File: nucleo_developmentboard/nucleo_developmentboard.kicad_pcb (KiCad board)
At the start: 2 copper layers, 91.4 x 69.8 mm, 30 parts, among them J1 Conn_01x03_Socket, J2 Conn_01x03_Socket, J3 Conn_01x02_Socket, J4 MOTOR2 OUT, J5 Conn_PinHeader_1x05_P2.54mm_V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, J6 MOTOR2 OUT, J7 Conn_01x01_Socket, J8 Conn_01x01_Socket, U1 NUCLEO-L432KC, U2 L293D, U3 LM7805_TO220, U4 HM-11_Module

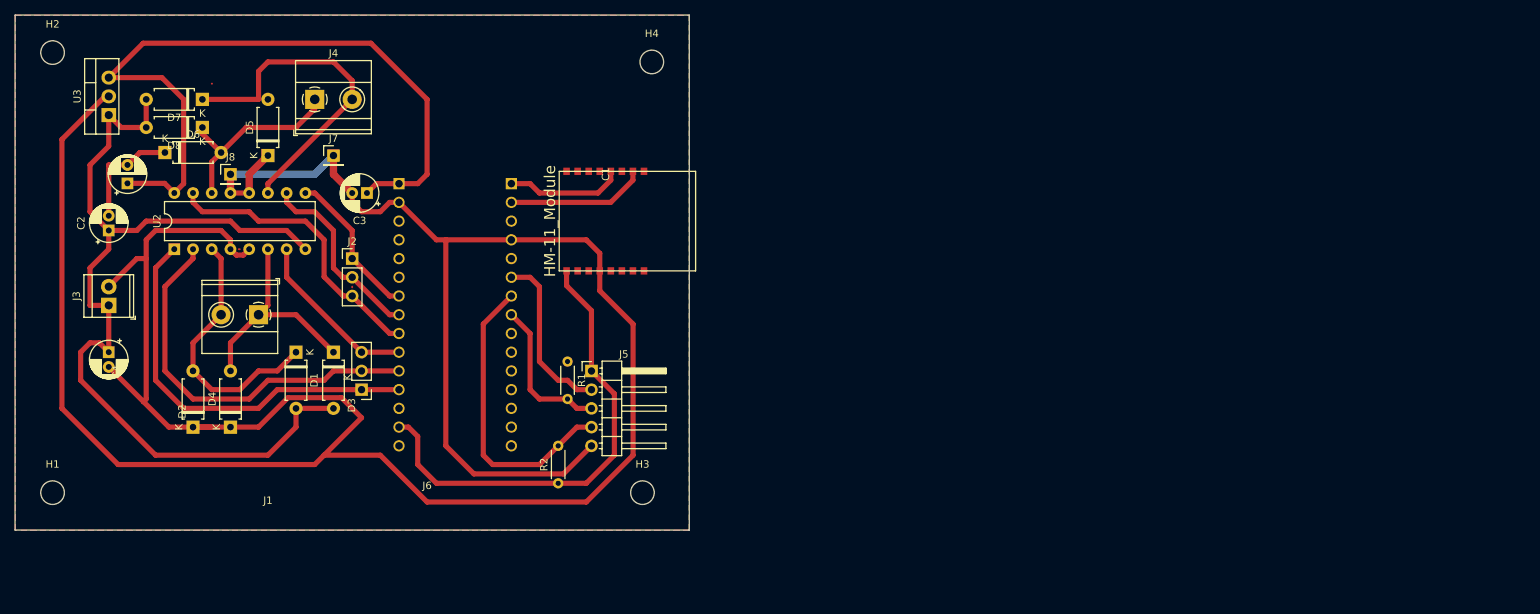
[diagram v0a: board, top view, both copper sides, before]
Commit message: updated Nucleo connections and switched to HM11 smd
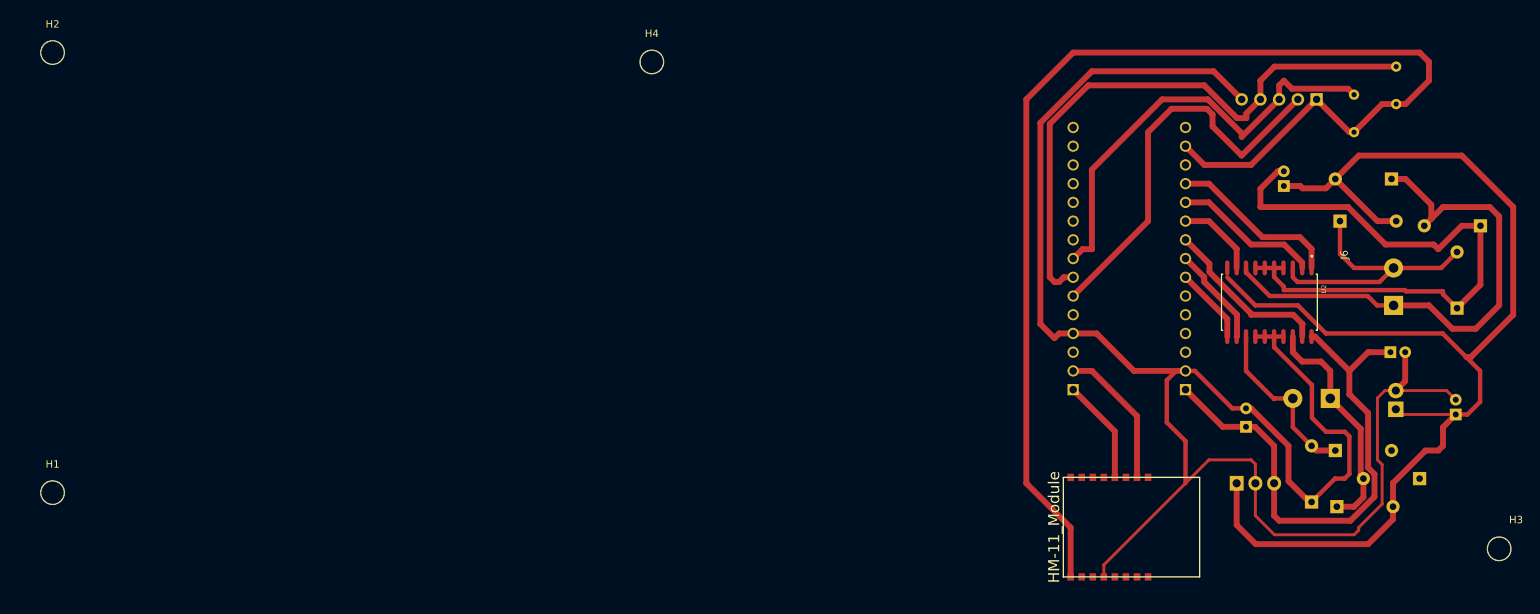
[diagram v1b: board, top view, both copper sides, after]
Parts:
- removed J1, J2: Conn_01x03_Socket, Connector_PinHeader_2.54mm:PinHeader_1x03_P2.54mm_Vertical
- removed J7, J8: Conn_01x01_Socket, Connector_PinHeader_2.54mm:PinHeader_1x01_P2.54mm_Vertical
- C1, C2, C3, C4, D1, D2, D3, D4, D5, D6, D7, D8, J3, J4, J5, J6, R1, R2, U3: moved to B.Cu
- U2: footprint Package_DIP:DIP-16_W7.62mm -> L293dd:SOIC127P1032X265-20N
- moved C2 184.4 mm to (250.0, 97.3)
- moved D6 175.8 mm to (245.1, 106.0), turned to 180 degrees
- moved J3 175.1 mm to (241.9, 96.6)
- moved D2 172.2 mm to (250.2, 82.9)
- moved D4 171.7 mm to (253.4, 71.8), turned to 180 degrees
- moved D8 162.2 mm to (233.9, 109.9), turned to 0 degrees
- moved C4 161.0 mm to (226.7, 66.4), turned to 90 degrees
- moved U3 160.9 mm to (220.3, 106.7), turned to 0 degrees
- moved D7 160.9 mm to (233.7, 102.2), turned to 0 degrees
- moved C1 155.3 mm to (221.6, 99.0)
- moved J6 154.0 mm to (241.6, 82.6), turned to 90 degrees
- moved D5 149.2 mm to (230.5, 109.2)
- moved U2 148.7 mm to (224.7, 82.1), turned to -90 degrees
- moved D3 145.4 mm to (241.3, 65.4), turned to 180 degrees
- moved J4 143.6 mm to (233.0, 95.2), turned to 180 degrees
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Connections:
- U2 pad 10: B_H -> +BAT
- U2 pad 11: Net-(D5-A) -> EN_B
- U2 pad 12: GND -> B_H
- U2 pad 13: GND -> Net-(D5-A)
- U2 pad 14: Net-(D6-A) -> GND
- U2 pad 15: B_L -> GND
- U2 pad 16: VCC -> GND
- U2 pad 6: Net-(D3-K) -> GND
- U2 pad 7: A_L -> GND
- U2 pad 8: +BAT -> Net-(D3-K)
- U2 pad 9: EN_B -> A_L
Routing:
- net 3V3: track 63.9 -> 170.1 mm
- net GND: track 394.2 -> 334.3 mm
- net +BAT: track 127.5 -> 174.2 mm
- net Net-(D3-K): track 30.9 -> 72.0 mm
- net SCL: track 20.6 -> 60.8 mm
- net SDA: track 40.5 -> 80.3 mm
- net A_H: track 53.0 -> 19.9 mm
- net XSHUT: track 23.1 -> 54.8 mm
- net EN_A: track 54.5 -> 23.3 mm
- net VCC: track 99.1 -> 72.0 mm
- net Net-(D5-A): track 45.7 -> 23.6 mm
- net B_L: track 39.5 -> 23.1 mm
- net B_H: track 25.8 -> 13.5 mm
- net A_L: track 23.3 -> 11.1 mm
- net EN_B: track 20.7 -> 10.4 mm
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- removed copper zone on F.Cu, net GND
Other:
- board outline removed
